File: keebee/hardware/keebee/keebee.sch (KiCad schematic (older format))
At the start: 7 parts, among them J1 USB_B_Micro, U1 LM1117-3.3, U2 STM32F042K6Tx

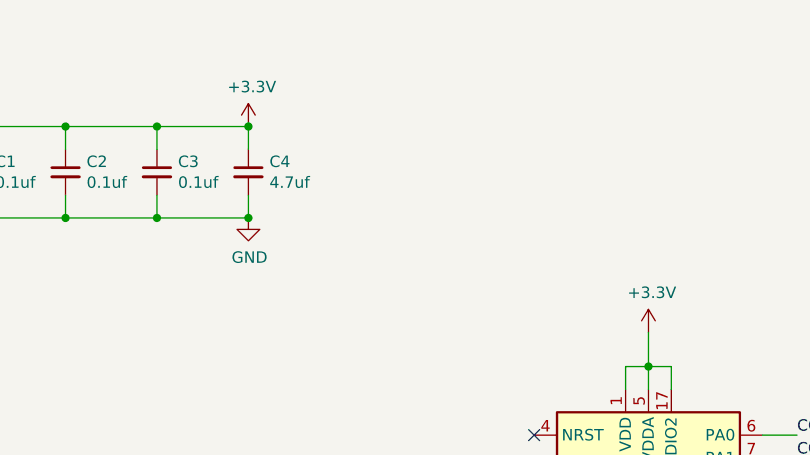
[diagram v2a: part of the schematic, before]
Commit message: Assign footprints and generate initial netlist.
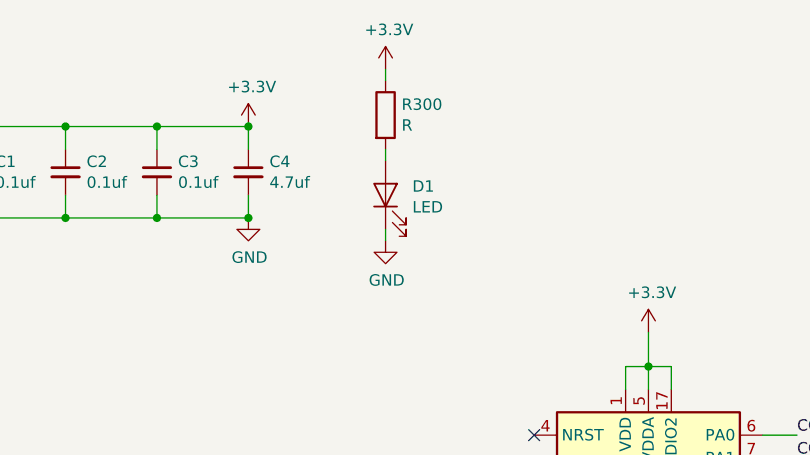
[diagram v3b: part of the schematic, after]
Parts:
- added D1: LED, LEDs:LED_0805_HandSoldering, symbol Device:LED
- added R300: R, Resistors_SMD:R_0805_HandSoldering, symbol Device:R
- C1, C2, C3, C4: footprint (none) -> Capacitors_SMD:C_0805_HandSoldering
- J1: footprint (none) -> custom_connectors:10118192-0001LF
- U1: footprint (none) -> TO_SOT_Packages_SMD:SOT-223
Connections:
- net +3V3: now also R300.1
- net GND: now also D1.1 (K)
- new net: D1.2 (A), R300.2
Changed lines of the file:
@@
 F 0 "J1" H 7371 3598 50  0000 R CNN
 F 1 "USB_B_Micro" H 7371 3689 50  0000 R CNN
-F 2 "" H 7750 3650 50  0001 C CNN
+F 2 "custom_connectors:10118192-0001LF" H 7750 3650 50  0001 C CNN
 F 3 "~" H 7750 3650 50  0001 C CNN
 	1    7600 3700
@@
 F 0 "U1" H 2050 1392 50  0000 C CNN
 F 1 "LM1117-3.3" H 2050 1301 50  0000 C CNN
-F 2 "" H 2050 1150 50  0001 C CNN
+F 2 "TO_SOT_Packages_SMD:SOT-223" H 2050 1150 50  0001 C CNN
 F 3 "http://www.ti.com/lit/ds/symlink/lm1117.pdf" H 2050 1150 50  0001 C CNN
 	1    2050 1150
@@
 F 0 "C1" H 2642 1396 50  0000 L CNN
 F 1 "0.1uf" H 2642 1305 50  0000 L CNN
-F 2 "" H 2550 1350 50  0001 C CNN
+F 2 "Capacitors_SMD:C_0805_HandSoldering" H 2550 1350 50  0001 C CNN
 F 3 "~" H 2550 1350 50  0001 C CNN
 	1    2550 1350
@@
 F 0 "C2" H 3042 1396 50  0000 L CNN
 F 1 "0.1uf" H 3042 1305 50  0000 L CNN
-F 2 "" H 2950 1350 50  0001 C CNN
+F 2 "Capacitors_SMD:C_0805_HandSoldering" H 2950 1350 50  0001 C CNN
 F 3 "~" H 2950 1350 50  0001 C CNN
 	1    2950 1350
@@
 F 0 "C3" H 3442 1396 50  0000 L CNN
 F 1 "0.1uf" H 3442 1305 50  0000 L CNN
-F 2 "" H 3350 1350 50  0001 C CNN
+F 2 "Capacitors_SMD:C_0805_HandSoldering" H 3350 1350 50  0001 C CNN
 F 3 "~" H 3350 1350 50  0001 C CNN
 	1    3350 1350
@@
 F 0 "C4" H 3842 1396 50  0000 L CNN
 F 1 "4.7uf" H 3842 1305 50  0000 L CNN
-F 2 "" H 3750 1350 50  0001 C CNN
+F 2 "Capacitors_SMD:C_0805_HandSoldering" H 3750 1350 50  0001 C CNN
 F 3 "~" H 3750 1350 50  0001 C CNN
 	1    3750 1350
@@
 Text Label 1800 3600 2    50   ~ 0
 ROW4
+$Comp
+L Device:LED D1
+U 1 1 5B7F9649
+P 4350 1450
+F 0 "D1" V 4388 1333 50  0000 R CNN
+F 1 "LED" V 4297 1333 50  0000 R CNN
+F 2 "LEDs:LED_0805_HandSoldering" H 4350 1450 50  0001 C CNN
+F 3 "~" H 4350 1450 50  0001 C CNN
+	1    4350 1450
+	0    -1   -1   0
+$EndComp
+$Comp
+L power:+3.3V #PWR0107
+U 1 1 5B7FBB10
+P 4350 900
+F 0 "#PWR0107" H 4350 750 50  0001 C CNN
+F 1 "+3.3V" H 4365 1073 50  0000 C CNN
+F 2 "" H 4350 900 50  0001 C CNN
+F 3 "" H 4350 900 50  0001 C CNN
+	1    4350 900
+	1    0    0    -1
+$EndComp
+$Comp
+L power:GND #PWR0108
+U 1 1 5B7FDF4E
+P 4350 1650
+F 0 "#PWR0108" H 4350 1400 50  0001 C CNN
+F 1 "GND" H 4355 1477 50  0000 C CNN
+F 2 "" H 4350 1650 50  0001 C CNN
+F 3 "" H 4350 1650 50  0001 C CNN
+	1    4350 1650
+	1    0    0    -1
+$EndComp
+$Comp
+L Device:R R300
+U 1 1 5B7FDFA5
+P 4350 1100
+F 0 "R300" H 4420 1146 50  0000 L CNN
+F 1 "R" H 4420 1055 50  0000 L CNN
+F 2 "Resistors_SMD:R_0805_HandSoldering" V 4280 1100 50  0001 C CNN
+F 3 "~" H 4350 1100 50  0001 C CNN
+	1    4350 1100
+	1    0    0    -1
+$EndComp
+Wire Wire Line
+	4350 950  4350 900
+Wire Wire Line
+	4350 1250 4350 1300
+Wire Wire Line
+	4350 1600 4350 1650
 $EndSCHEMATC

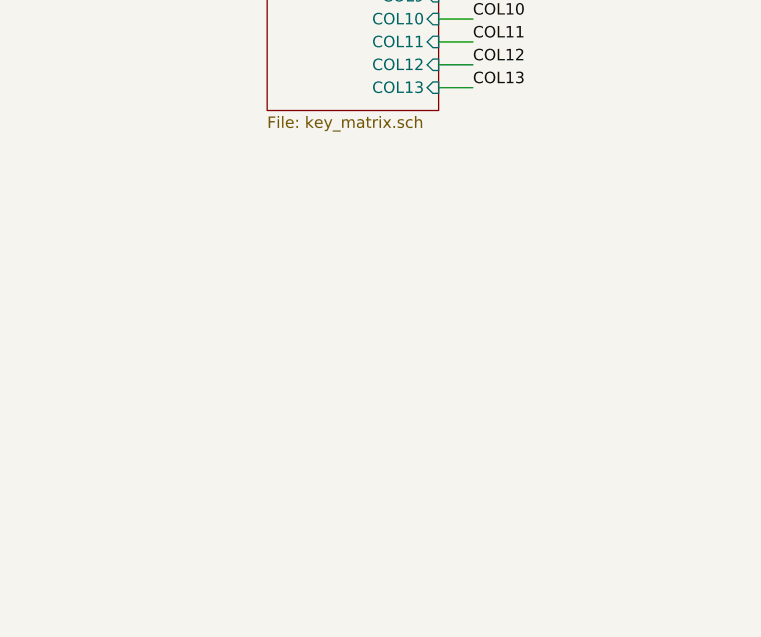
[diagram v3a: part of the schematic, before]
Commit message: Add JTAG connector.
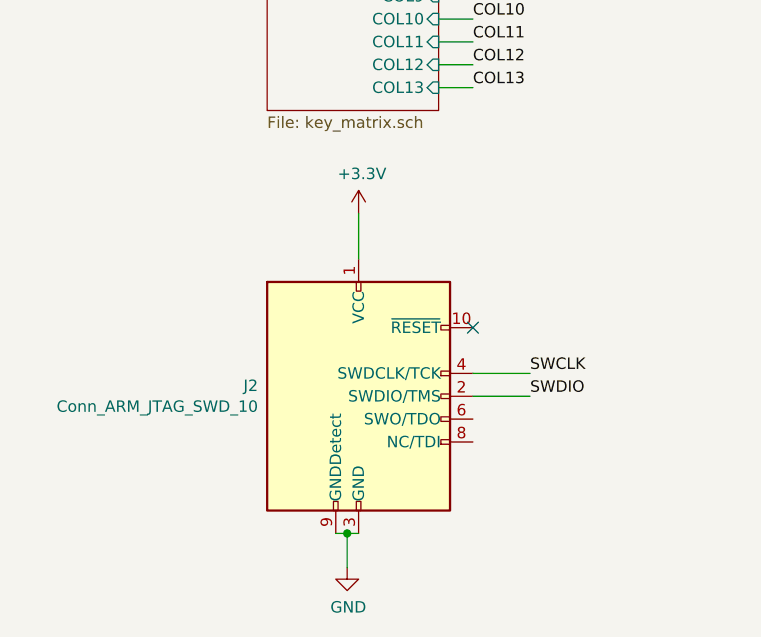
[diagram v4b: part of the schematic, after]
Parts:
- added J2: Conn_ARM_JTAG_SWD_10, Connector_PinHeader_1.27mm:PinHeader_2x05_P1.27mm_Vertical_SMD, symbol Connector:Conn_ARM_JTAG_SWD_10
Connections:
- net +3V3: now also J2.1 (VCC)
- net GND: now also J2.3 (GND), J2.5 (GND), J2.9 (GNDDetect)
- net SWCLK: now also J2.4 (SWDCLK/TCK)
- net SWDIO: now also J2.2 (SWDIO/TMS)
- no-connect marks 6 -> 7
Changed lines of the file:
@@
 Wire Wire Line
 	4350 1600 4350 1650
+$Comp
+L Connector:Conn_ARM_JTAG_SWD_10 J2
+U 1 1 5B8052BF
+P 2350 5850
+F 0 "J2" H 1910 5896 50  0000 R CNN
+F 1 "Conn_ARM_JTAG_SWD_10" H 1910 5805 50  0000 R CNN
+F 2 "Connector_PinHeader_1.27mm:PinHeader_2x05_P1.27mm_Vertical_SMD" H 2400 5300 50  0001 L TNN
+F 3 "http://infocenter.arm.com/help/topic/com.arm.doc.faqs/attached/13634/cortex_debug_connectors.pdf" V 2000 4600 50  0001 C CNN
+	1    2350 5850
+	1    0    0    -1
+$EndComp
+Wire Wire Line
+	2350 5250 2350 5050
+$Comp
+L power:+3.3V #PWR02
+U 1 1 5B810A79
+P 2350 5050
+F 0 "#PWR02" H 2350 4900 50  0001 C CNN
+F 1 "+3.3V" H 2365 5223 50  0000 C CNN
+F 2 "" H 2350 5050 50  0001 C CNN
+F 3 "" H 2350 5050 50  0001 C CNN
+	1    2350 5050
+	1    0    0    -1
+$EndComp
+Wire Wire Line
+	2250 6450 2300 6450
+Wire Wire Line
+	2300 6450 2300 6600
+Connection ~ 2300 6450
+Wire Wire Line
+	2300 6450 2350 6450
+$Comp
+L power:GND #PWR01
+U 1 1 5B81573F
+P 2300 6600
+F 0 "#PWR01" H 2300 6350 50  0001 C CNN
+F 1 "GND" H 2305 6427 50  0000 C CNN
+F 2 "" H 2300 6600 50  0001 C CNN
+F 3 "" H 2300 6600 50  0001 C CNN
+	1    2300 6600
+	1    0    0    -1
+$EndComp
+NoConn ~ 2850 5550
+Wire Wire Line
+	2850 5750 3100 5750
+Text Label 3100 5750 0    50   ~ 0
+SWCLK
+Wire Wire Line
+	2850 5850 3100 5850
+Text Label 3100 5850 0    50   ~ 0
+SWDIO
 $EndSCHEMATC

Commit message: Add layout switch.
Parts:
- added SW_LO: SW_SPST, symbol Switch:SW_SPST
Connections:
- net GND: now also SW_LO.1 (A)
- net at U2.31 (PB8): now also SW_LO.2 (B)
- no-connect marks 7 -> 6
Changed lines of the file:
@@
 NoConn ~ 5000 3000
 NoConn ~ 5000 3100
-NoConn ~ 5000 4000
 Text Label 4700 3300 0    50   ~ 0
 COL8
@@
 Text Label 3100 5850 0    50   ~ 0
 SWDIO
+Wire Wire Line
+	5000 4000 4400 4000
+$Comp
+L Switch:SW_SPST SW_LO
+U 1 1 5D241928
+P 4200 4000
+F 0 "SW_LO" H 4200 4235 50  0000 C CNN
+F 1 "SW_SPST" H 4200 4144 50  0000 C CNN
+F 2 "" H 4200 4000 50  0001 C CNN
+F 3 "" H 4200 4000 50  0001 C CNN
+	1    4200 4000
+	1    0    0    -1
+$EndComp
+Wire Wire Line
+	4000 4000 3850 4000
+Wire Wire Line
+	3850 4000 3850 4250
+$Comp
+L power:GND #PWR?
+U 1 1 5D244BDB
+P 3850 4250
+F 0 "#PWR?" H 3850 4000 50  0001 C CNN
+F 1 "GND" H 3855 4077 50  0000 C CNN
+F 2 "" H 3850 4250 50  0001 C CNN
+F 3 "" H 3850 4250 50  0001 C CNN
+	1    3850 4250
+	1    0    0    -1
+$EndComp
 $EndSCHEMATC
